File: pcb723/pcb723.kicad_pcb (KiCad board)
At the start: 4 copper layers, 90 x 70 mm, 71 parts, among them J1 Conn_01x02_Pin, J10 Conn_01x05_Socket, J11 Conn_01x05_Socket, J2 Conn_01x02_Pin, J3 Conn_02x07_Odd_Even, J4 Conn_02x02_Odd_Even, J5 USB_C_Receptacle_USB2.0_16P, J6 Conn_02x13_Odd_Even, J7 Conn_02x14_Odd_Even, J8 Conn_02x13_Odd_Even, J9 Conn_02x12_Odd_Even, SW1 SW_Push, U1 STM32H723ZGT6, U2 AMS1117-3.3, Y1 8MHz 20pF

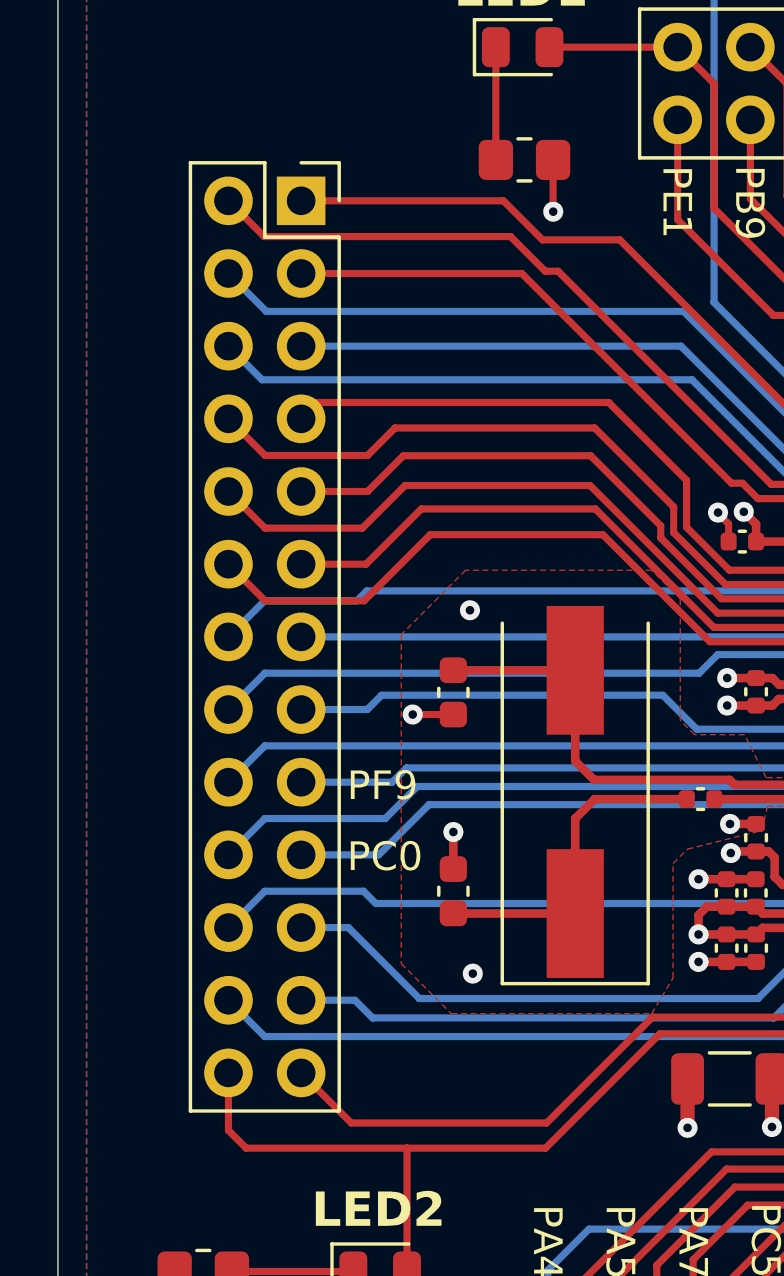
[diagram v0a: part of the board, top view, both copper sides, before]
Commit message: Label LED2
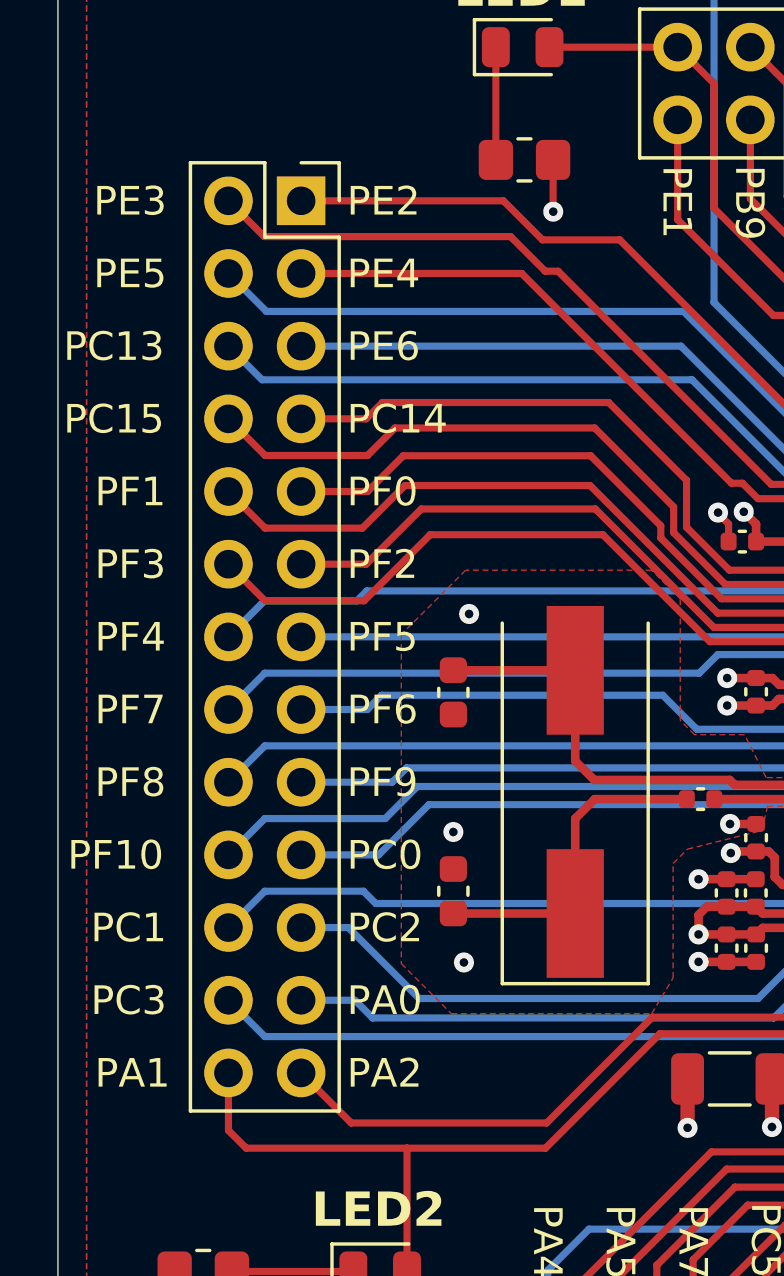
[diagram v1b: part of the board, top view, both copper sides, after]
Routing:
- net GND: track 71.9 -> 69.2 mm, vias 41 -> 40
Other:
- board text added: "PA0"
- board text added: "PA1"
- board text added: "PA2"
- board text added: "PC1"
- board text added: "PC13"
- board text added: "PC14"
- board text added: "PC15"
- board text added: "PC2"
- board text added: "PC3"
- board text added: "PE2"
- board text added: "PE3"
- board text added: "PE4"
- board text added: "PE5"
- board text added: "PE6"
- board text added: "PF0"
- board text added: "PF1"
- board text added: "PF10"
- board text added: "PF2"
- board text added: "PF3"
- board text added: "PF4"
- board text added: "PF5"
- board text added: "PF6"
- board text added: "PF7"
- board text added: "PF8"

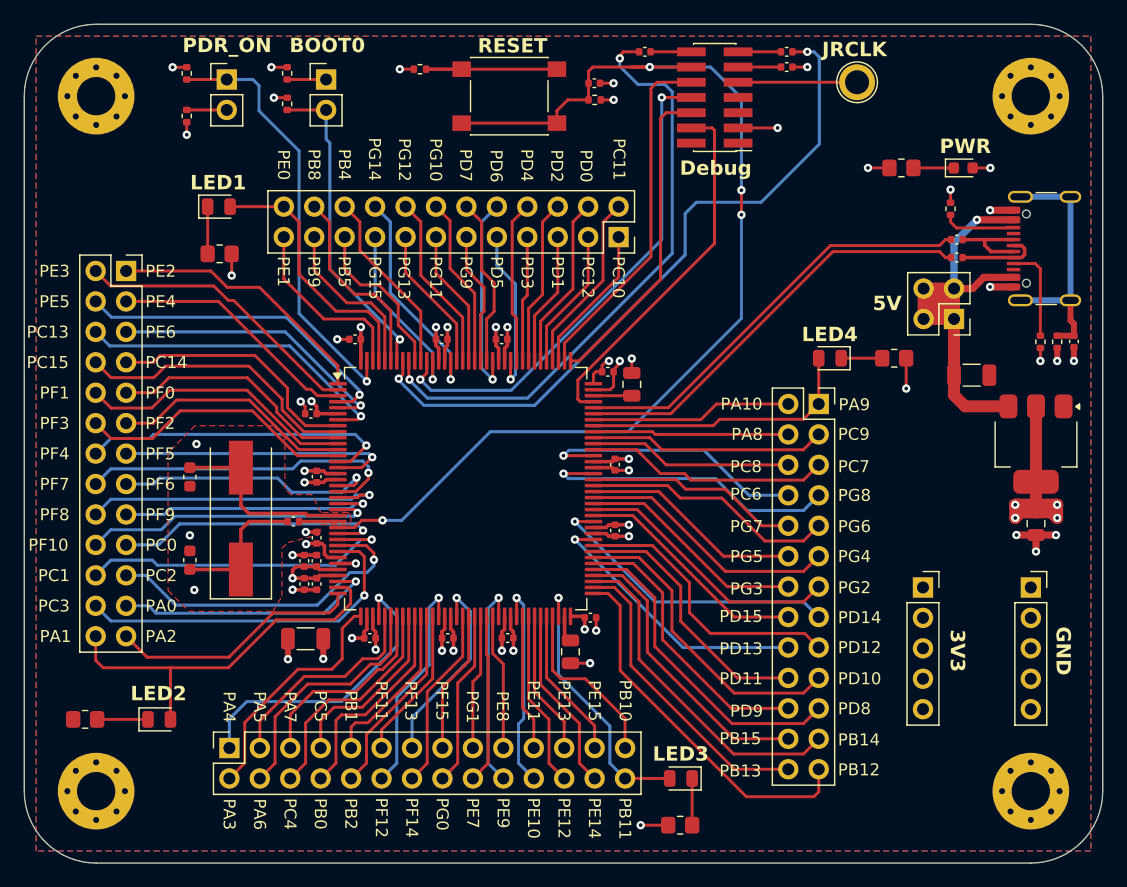
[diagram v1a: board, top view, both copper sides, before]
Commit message: Thermal relief zones
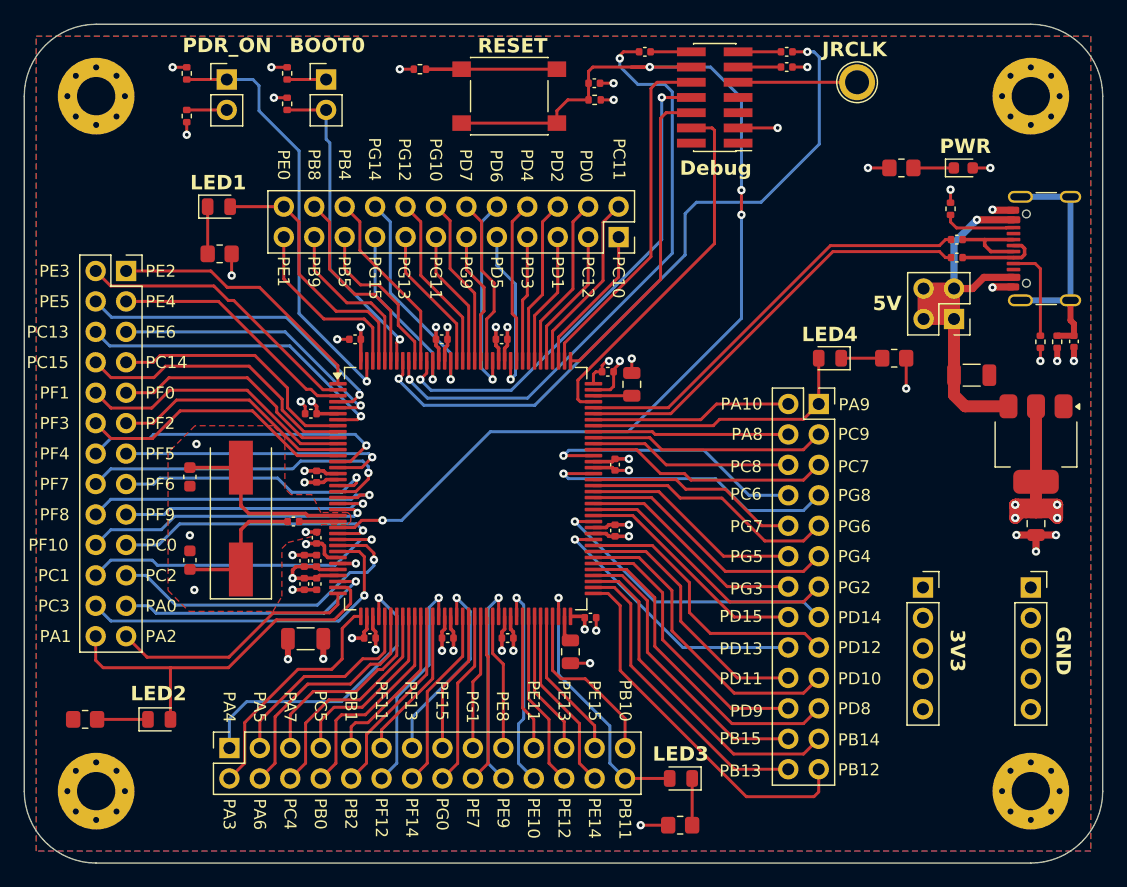
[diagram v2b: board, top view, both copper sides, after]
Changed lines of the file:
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@@
 	)
 	(footprint "Connector_USB:USB_C_Receptacle_GCT_USB4105-xx-A_16P_TopMnt_Horizontal"
+		(locked yes)
 		(layer "F.Cu")
 		(at 176.235 58.72 90)
@@
 			)
 		)
-		(property ki_fp_filters "USB*C*Receptacle*")
-		(sheetname "Root")
-		(sheetfile "pcb723.kicad_sch")
 		(attr smd)
 		(fp_line
@@
 		)
 		(pad "A1" smd roundrect
-			(at -3.2 -3.68 90)
-			(size 0.6 1.15)
+			(at -3.2 -3.7275 90)
+			(size 0.6 1.055)
 			(layers "F.Cu" "F.Paste" "F.Mask")
 			(roundrect_rratio 0.25)
@@
 		)
 		(pad "A12" smd roundrect
-			(at 3.2 -3.68 90)
-			(size 0.6 1.15)
+			(at 3.2 -3.7275 90)
+			(size 0.6 1.055)
 			(layers "F.Cu" "F.Paste" "F.Mask")
 			(roundrect_rratio 0.25)
@@
 		)
 		(pad "B1" smd roundrect
-			(at 3.2 -3.68 90)
-			(size 0.6 1.15)
+			(at 3.2 -3.7275 90)
+			(size 0.6 1.055)
 			(layers "F.Cu" "F.Paste" "F.Mask")
 			(roundrect_rratio 0.25)
@@
 		)
 		(pad "B12" smd roundrect
-			(at -3.2 -3.68 90)
-			(size 0.6 1.15)
+			(at -3.2 -3.7275 90)
+			(size 0.6 1.055)
 			(layers "F.Cu" "F.Paste" "F.Mask")
 			(roundrect_rratio 0.25)
@@
 	)
 	(segment
-		(start 137.73 89.52)
-		(end 137.73 90.6)
-		(width 0.25)
+		(start 170.85 61.92)
+		(end 172.5075 61.92)
+		(width 0.6)
 		(layer "F.Cu")
 		(net 29)
 	)
 	(segment
-		(start 172.555 55.52)
-		(end 170.6 55.52)
-		(width 0.6)
+		(start 137.73 89.52)
+		(end 137.73 90.6)
+		(width 0.25)
 		(layer "F.Cu")
 		(net 29)
@@
 	)
 	(segment
-		(start 172.555 61.92)
-		(end 170.6 61.92)
-		(width 0.6)
-		(layer "F.Cu")
-		(net 29)
-	)
-	(segment
 		(start 124.86 90.69)
 		(end 125.0875 90.4625)
@@
 	)
 	(segment
+		(start 170.85 55.52)
+		(end 172.5075 55.52)
+		(width 0.6)
+		(layer "F.Cu")
+		(net 29)
+	)
+	(segment
 		(start 125.0875 90.4625)
 		(end 125.0875 89.4125)
@@
 	)
 	(segment
+		(start 170.8 61.97)
+		(end 170.85 61.92)
+		(width 0.6)
+		(layer "F.Cu")
+		(net 29)
+	)
+	(segment
 		(start 114.955 91.28)
 		(end 114.955 92.96)
@@
 		(net 29)
 	)
+	(segment
+		(start 170.8 55.47)
+		(end 170.85 55.52)
+		(width 0.6)
+		(layer "F.Cu")
+		(net 29)
+	)
 	(via
 		(at 137.22 93.32)
@@
 	)
 	(via
-		(at 170.6 61.92)
+		(at 170.8 61.97)
 		(size 0.7)
 		(drill 0.3)
@@
 	)
 	(via
-		(at 170.6 55.52)
+		(at 170.8 55.47)
 		(size 0.7)
 		(drill 0.3)
@@
 	)
 	(segment
-		(start 126.62 93.59)
-		(end 127.23 92.98)
-		(width 0.25)
-		(layer "B.Cu")
-		(net 76)
-	)
-	(segment
-		(start 126.62 93.59)
-		(end 126.73 93.48)
-		(width 0.25)
-		(layer "B.Cu")
-		(net 76)
-	)
-	(segment
 		(start 127.23 92.98)
 		(end 127.23 89.0125)
@@
 	(segment
 		(start 122.36 97.85)
-		(end 126.62 93.59)
+		(end 127.23 92.98)
 		(width 0.25)
 		(layer "B.Cu")
@@
 	)
 	(zone
+		(net 0)
+		(net_name "")
+		(layer "F.Cu")
+		(name "Thermal")
+		(hatch edge 0.5)
+		(connect_pads
+			(clearance 0)
+		)
+		(min_thickness 0.25)
+		(filled_areas_thickness no)
+		(keepout
+			(tracks allowed)
+			(vias allowed)
+			(pads allowed)
+			(copperpour not_allowed)
+			(footprints allowed)
+		)
+		(fill
+			(thermal_gap 0.5)
+			(thermal_bridge_width 0.5)
+		)
+		(polygon
+			(pts
+				(xy 171.9 55.3) (xy 171.5 55.3) (xy 171.5 55.5) (xy 171.9 55.5)
+			)
+		)
+	)
+	(zone
 		(net 29)
 		(net_name "GND")
@@
 			)
 		)
+	)
+	(zone
+		(net 0)
+		(net_name "")
+		(layer "F.Cu")
+		(name "Thermal")
+		(hatch edge 0.5)
+		(connect_pads
+			(clearance 0)
+		)
+		(min_thickness 0.25)
+		(filled_areas_thickness no)
+		(keepout
+			(tracks allowed)
+			(vias allowed)
+			(pads allowed)
+			(copperpour not_allowed)
+			(footprints allowed)
+		)
+		(fill
+			(thermal_gap 0.5)
+			(thermal_bridge_width 0.5)
+		)
+		(polygon
+			(pts
+				(xy 171.3 61.9) (xy 171.9 61.9) (xy 171.9 62.2) (xy 171.3 62.2)
+			)
+		)

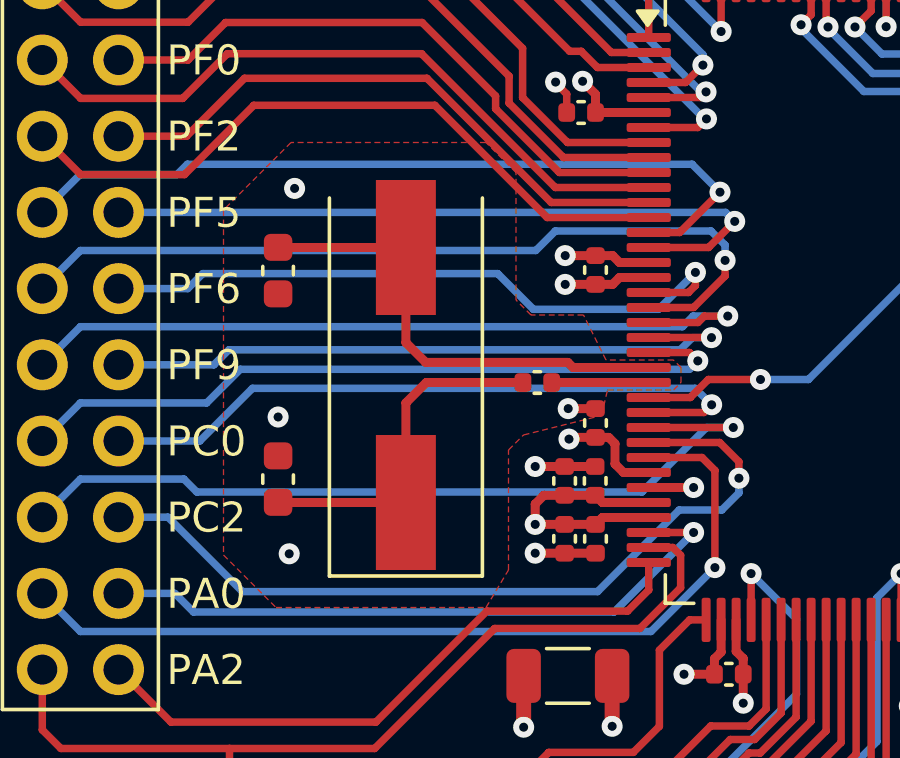
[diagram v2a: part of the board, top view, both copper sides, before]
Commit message: Replace 8MHz
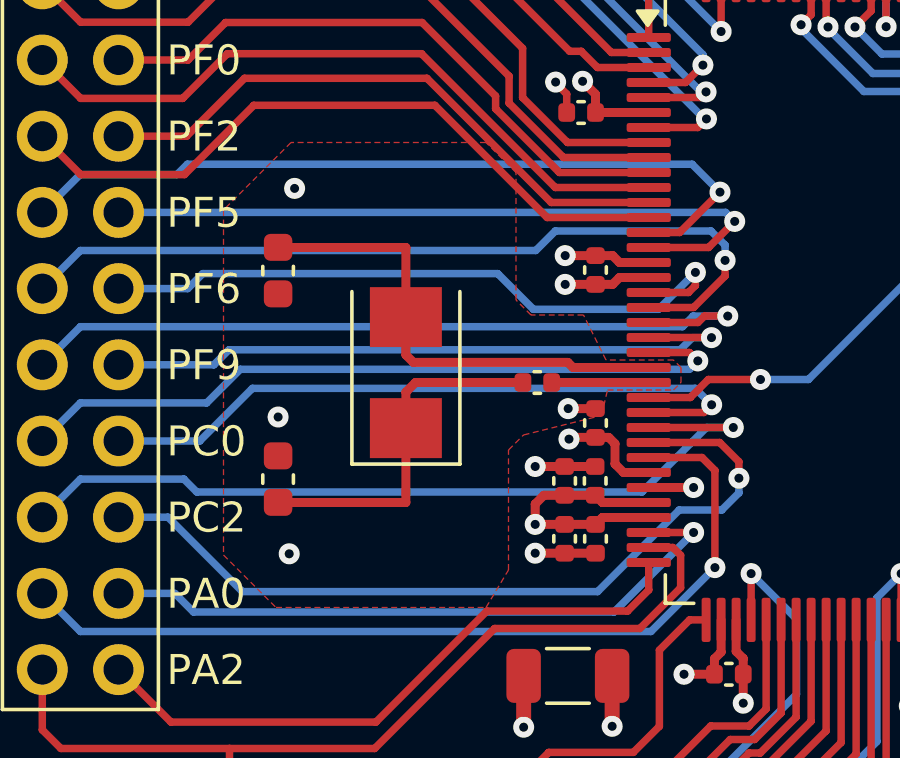
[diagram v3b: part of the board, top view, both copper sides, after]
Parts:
- Y1: footprint Crystal:Crystal_SMD_HC49-SD -> Crystal:Crystal_SMD_5032-2Pin_5.0x3.2mm
- moved Y1 0.08 mm to (108.1, 81.2)
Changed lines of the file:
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@@
 		)
 	)
-	(footprint "Crystal:Crystal_SMD_HC49-SD"
+	(footprint "Crystal:Crystal_SMD_5032-2Pin_5.0x3.2mm"
 		(layer "F.Cu")
-		(at 108.08 81.25 90)
-		(descr "SMD Crystal HC-49-SD http://cdn-reichelt.de/documents/datenblatt/B400/xxx-HC49-SMD.pdf, 11.4x4.7mm^2 package")
+		(at 108.08 81.17 90)
+		(descr "SMD Crystal SERIES SMD2520/2 http://www.icbase.com/File/PDF/HKC/HKC00061008.pdf, 5.0x3.2mm^2 package")
 		(tags "SMD SMT crystal")
 		(property "Reference" "Y1"
-			(at 0 -3.55 -90)
+			(at 0 -2.8 90)
 			(layer "F.SilkS")
 			(hide yes)
@@
 		)
 		(property "Value" "8MHz 20pF"
-			(at 0 3.55 -90)
+			(at 0 2.8 90)
 			(layer "F.Fab")
 			(hide yes)
@@
 			)
 		)
-		(property "Footprint" "Crystal:Crystal_SMD_HC49-SD"
+		(property "Footprint" "Crystal:Crystal_SMD_5032-2Pin_5.0x3.2mm"
 			(at 0 0 90)
 			(unlocked yes)
@@
 			)
 		)
-		(property "JLC#" "C12674"
+		(property "JLC#" "C115962"
 			(at 0 0 90)
 			(unlocked yes)
@@
 		(sheetfile "pcb723.kicad_sch")
 		(attr smd)
+		(fp_circle
+			(center 0 0)
+			(end 0.4 0)
+			(stroke
+				(width 0.1)
+				(type solid)
+			)
+			(fill none)
+			(layer "F.Adhes")
+		)
+		(fp_circle
+			(center 0 0)
+			(end 0.333333 0)
+			(stroke
+				(width 0.133333)
+				(type solid)
+			)
+			(fill none)
+			(layer "F.Adhes")
+		)
+		(fp_circle
+			(center 0 0)
+			(end 0.213333 0)
+			(stroke
+				(width 0.133333)
+				(type solid)
+			)
+			(fill none)
+			(layer "F.Adhes")
+		)
+		(fp_circle
+			(center 0 0)
+			(end 0.093333 0)
+			(stroke
+				(width 0.186667)
+				(type solid)
+			)
+			(fill none)
+			(layer "F.Adhes")
+		)
 		(fp_line
-			(start 5.9 -2.55)
-			(end -6.7 -2.55)
+			(start 2.7 -1.8)
+			(end -3.05 -1.8)
 			(stroke
 				(width 0.12)
@@
 		)
 		(fp_line
-			(start -6.7 -2.55)
-			(end -6.7 2.55)
+			(start -3.05 -1.8)
+			(end -3.05 1.8)
 			(stroke
 				(width 0.12)
@@
 		)
 		(fp_line
-			(start -6.7 2.55)
-			(end 5.9 2.55)
+			(start -3.05 1.8)
+			(end 2.7 1.8)
 			(stroke
 				(width 0.12)
@@
 		)
 		(fp_line
-			(start 6.8 -2.6)
-			(end -6.8 -2.6)
+			(start 3.1 -1.9)
+			(end -3.1 -1.9)
 			(stroke
 				(width 0.05)
@@
 		)
 		(fp_line
-			(start -6.8 -2.6)
-			(end -6.8 2.6)
+			(start -3.1 -1.9)
+			(end -3.1 1.9)
 			(stroke
 				(width 0.05)
@@
 		)
 		(fp_line
-			(start 6.8 2.6)
-			(end 6.8 -2.6)
+			(start 3.1 1.9)
+			(end 3.1 -1.9)
 			(stroke
 				(width 0.05)
@@
 		)
 		(fp_line
-			(start -6.8 2.6)
-			(end 6.8 2.6)
+			(start -3.1 1.9)
+			(end 3.1 1.9)
 			(stroke
 				(width 0.05)
@@
 		)
 		(fp_line
-			(start 5.7 -2.35)
-			(end -5.7 -2.35)
+			(start 2.3 -1.6)
+			(end 2.5 -1.4)
+			(stroke
+				(width 0.1)
+				(type solid)
+			)
+			(layer "F.Fab")
+		)
+		(fp_line
+			(start -2.3 -1.6)
+			(end 2.3 -1.6)
 			(stroke
 				(width 0.1)
@@
 		)
 		(fp_line
-			(start -5.7 -2.35)
-			(end -5.7 2.35)
+			(start 2.5 -1.4)
+			(end 2.5 1.4)
 			(stroke
 				(width 0.1)
@@
 		)
 		(fp_line
-			(start -3.015 -2.115)
-			(end 3.015 -2.115)
+			(start -2.5 -1.4)
+			(end -2.3 -1.6)
 			(stroke
 				(width 0.1)
@@
 		)
 		(fp_line
-			(start -3.015 2.115)
-			(end 3.015 2.115)
+			(start -2.5 0.6)
+			(end -1.5 1.6)
 			(stroke
 				(width 0.1)
@@
 		)
 		(fp_line
-			(start 5.7 2.35)
-			(end 5.7 -2.35)
+			(start 2.5 1.4)
+			(end 2.3 1.6)
 			(stroke
 				(width 0.1)
@@
 		)
 		(fp_line
-			(start -5.7 2.35)
-			(end 5.7 2.35)
+			(start -2.5 1.4)
+			(end -2.5 -1.4)
 			(stroke
 				(width 0.1)
@@
 			(layer "F.Fab")
 		)
-		(fp_arc
-			(start 3.015 -2.115)
-			(mid 5.13 0)
-			(end 3.015 2.115)
+		(fp_line
+			(start 2.3 1.6)
+			(end -2.3 1.6)
 			(stroke
 				(width 0.1)
@@
 			(layer "F.Fab")
 		)
-		(fp_arc
-			(start -3.015 2.115)
-			(mid -5.13 0)
-			(end -3.015 -2.115)
+		(fp_line
+			(start -2.3 1.6)
+			(end -2.5 1.4)
 			(stroke
 				(width 0.1)
@@
 		)
 		(fp_text user "${REFERENCE}"
-			(at 0 0 -90)
+			(at 0 0 90)
 			(layer "F.Fab")
 			(effects
@@
 		)
 		(pad "1" smd rect
-			(at -4.25 0 90)
-			(size 4.5 2)
+			(at -1.85 0 90)
+			(size 2 2.4)
 			(layers "F.Cu" "F.Paste" "F.Mask")
 			(net 6 "Net-(C22-Pad1)")
@@
 		)
 		(pad "2" smd rect
-			(at 4.25 0 90)
-			(size 4.5 2)
+			(at 1.85 0 90)
+			(size 2 2.4)
 			(layers "F.Cu" "F.Paste" "F.Mask")
 			(net 14 "/PH0")
@@
 			(pintype "passive")
 		)
-		(model "${KICAD8_3DMODEL_DIR}/Crystal.3dshapes/Crystal_SMD_HC49-SD.wrl"
+		(model "${KICAD8_3DMODEL_DIR}/Crystal.3dshapes/Crystal_SMD_5032-2Pin_5.0x3.2mm.wrl"
 			(offset
 				(xyz 0 0 0)
@@
 			)
 		)
+		(property ki_fp_filters "USB*C*Receptacle*")
+		(sheetname "Root")
+		(sheetfile "pcb723.kicad_sch")
 		(attr smd)
 		(fp_line
@@
 	)
 	(segment
-		(start 108.76 81.5)
-		(end 111.98 81.5)
+		(start 108.08 81.82)
+		(end 108.4 81.5)
 		(width 0.3)
 		(layer "F.Cu")
@@
 	)
 	(segment
-		(start 108.08 85.5)
-		(end 108.08 82.18)
+		(start 108.4 81.5)
+		(end 111.98 81.5)
 		(width 0.3)
 		(layer "F.Cu")
@@
 	)
 	(segment
-		(start 103.82 85.495)
-		(end 103.825 85.5)
+		(start 108.08 85.5)
+		(end 108.08 81.82)
 		(width 0.3)
 		(layer "F.Cu")
@@
 	)
 	(segment
-		(start 108.08 82.18)
-		(end 108.76 81.5)
+		(start 103.82 85.495)
+		(end 103.825 85.5)
 		(width 0.3)
 		(layer "F.Cu")
@@
 	)
 	(segment
-		(start 113.48 80.83)
-		(end 108.74 80.83)
+		(start 108.08 77)
+		(end 103.825 77)
 		(width 0.3)
 		(layer "F.Cu")
@@
 	)
 	(segment
-		(start 108.74 80.83)
-		(end 108.08 80.17)
+		(start 108.33 80.83)
+		(end 108.08 80.58)
 		(width 0.3)
 		(layer "F.Cu")
@@
 	)
 	(segment
-		(start 116.175 81)
-		(end 113.65 81)
+		(start 113.65 81)
+		(end 113.48 80.83)
 		(width 0.3)
 		(layer "F.Cu")
@@
 	)
 	(segment
-		(start 103.825 77)
-		(end 103.82 76.995)
+		(start 113.48 80.83)
+		(end 108.33 80.83)
 		(width 0.3)
 		(layer "F.Cu")
@@
 	)
 	(segment
-		(start 108.08 77)
-		(end 103.825 77)
+		(start 108.08 80.58)
+		(end 108.08 77)
 		(width 0.3)
 		(layer "F.Cu")
@@
 	)
 	(segment
-		(start 113.65 81)
-		(end 113.48 80.83)
+		(start 103.825 77)
+		(end 103.82 76.995)
 		(width 0.3)
 		(layer "F.Cu")
@@
 	)
 	(segment
-		(start 108.08 80.17)
-		(end 108.08 77)
+		(start 116.175 81)
+		(end 113.65 81)
 		(width 0.3)
 		(layer "F.Cu")
